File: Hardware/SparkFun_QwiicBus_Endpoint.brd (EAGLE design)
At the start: 44.5 x 25.4 mm, 68 parts, among them J1 QWIIC, J2 QWIIC, J3 RJ45, U1 PCA9615

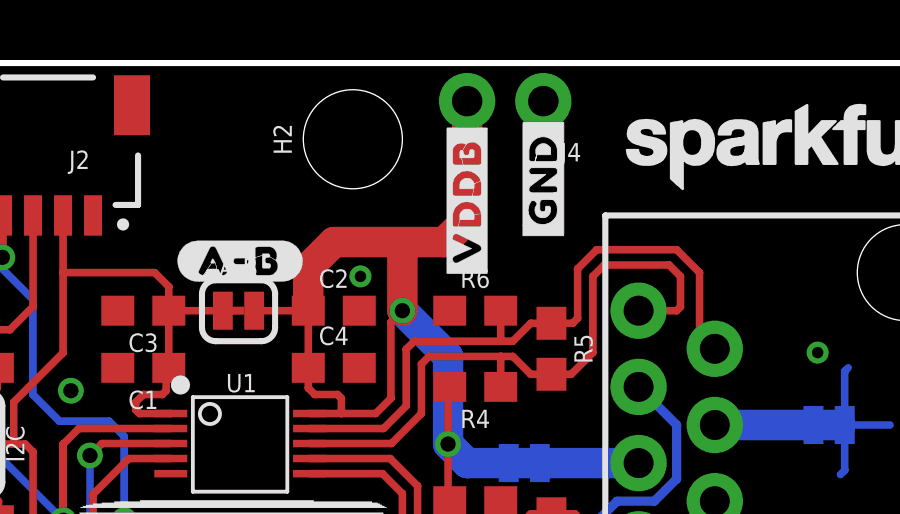
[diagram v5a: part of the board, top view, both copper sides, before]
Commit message: changing labels on grn pair, removing vddb
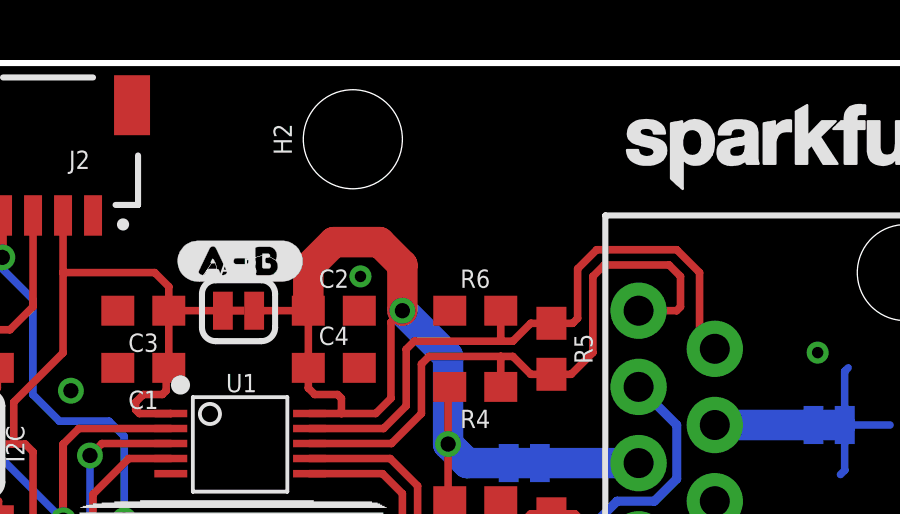
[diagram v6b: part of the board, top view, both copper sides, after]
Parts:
- removed J4: (no value), SparkFun-Connectors:1X02_NO_SILK
- removed U$12, U$13: (no value), output:#VDDB#0
- removed U$20: (no value), output:#GRNW#0
- removed U$22: (no value), output:#GRN#0
- U$2, U$3: device output:#GND#0 -> output:#HV##0
- moved U$3 22.1 mm to (26.7, 1.78), turned to 90 degrees
- moved U$2 17.5 mm to (29.2, 1.78), flipped to the bottom
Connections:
- net GND: no longer J4.1
- net VDD_B: no longer J4.2
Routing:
- net VDD_B: track 37.3 -> 30.5 mm
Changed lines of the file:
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@@
 <attribute name="VALUE" x="4.572" y="22.86" size="0.6096" layer="27" font="vector" ratio="20" rot="R90" align="top-center"/>
-</element>
-<element name="J4" library="SparkFun-Connectors" package="1X02_NO_SILK" value="" x="29.21" y="24.13" smashed="yes" rot="R180">
-<attribute name="NAME" x="30.48" y="22.733" size="0.6096" layer="25" font="vector" ratio="20" rot="R180"/>
-<attribute name="VALUE" x="30.48" y="26.162" size="0.6096" layer="27" font="vector" ratio="20" rot="R180"/>
 </element>
 <element name="LOGO1" library="SparkFun-Aesthetics" package="OSHW-LOGO-M" value="OSHW-LOGOM" x="12.7" y="2.54" smashed="yes" rot="MR0"/>
@@
 <attribute name="VALUE" x="25.4" y="-0.762" size="0.6096" layer="27" font="vector" ratio="20"/>
 </element>
-<element name="U$2" library="output" package="#GND#0" value="" x="29.21" y="19.304" smashed="yes" rot="R90"/>
-<element name="U$3" library="output" package="#GND#0" value="" x="29.21" y="23.749" smashed="yes" rot="MR270"/>
 <element name="U$4" library="output" package="#GND#0" value="" x="6.223" y="17.78" smashed="yes" rot="MR0"/>
 <element name="U$5" library="output" package="#GND#0" value="" x="1.778" y="17.78" smashed="yes"/>
@@
 <element name="U$10" library="output" package="#SCL#0" value="" x="1.778" y="10.16" smashed="yes"/>
 <element name="U$11" library="output" package="#EN#0" value="" x="1.778" y="7.62" smashed="yes"/>
-<element name="U$12" library="output" package="#VDDB#0" value="" x="26.67" y="18.034" smashed="yes" rot="R90"/>
-<element name="U$13" library="output" package="#VDDB#0" value="" x="26.67" y="18.034" smashed="yes" rot="MR90"/>
 <element name="U$14" library="output" package="#VDDB#0" value="" x="28.575" y="18.288" smashed="yes" rot="MR270"/>
 <element name="U$15" library="output" package="#SDA#0" value="" x="6.223" y="12.7" smashed="yes" rot="MR0"/>
@@
 <element name="U$18" library="output" package="#A#B#0" value="" x="17.018" y="18.796" smashed="yes"/>
 <element name="U$19" library="output" package="#GRNW#0" value="" x="29.21" y="1.905" smashed="yes" rot="R90"/>
-<element name="U$20" library="output" package="#GRNW#0" value="" x="29.21" y="7.747" smashed="yes" rot="MR270"/>
 <element name="U$21" library="output" package="#GRN#0" value="" x="26.67" y="2.032" smashed="yes" rot="R90"/>
-<element name="U$22" library="output" package="#GRN#0" value="" x="26.67" y="6.35" smashed="yes" rot="MR270"/>
 <element name="U$25" library="output" package="ENDPOINT0" value="" x="30.48" y="2.54" smashed="yes"/>
 <element name="U$26" library="output" package="ENDPOINT0" value="" x="25.781" y="9.525" smashed="yes" rot="MR0"/>
@@
 <element name="U$28" library="QwiicBus#working#Logo#jpg (2)" package="QWIICBUS#WORKING#LOGO#JPG" value="" x="19.558" y="8.509" smashed="yes"/>
 <element name="U$23" library="QwiicBus#working#Logo#jpg (2)" package="QWIICBUS#WORKING#LOGO#JPG" value="" x="18.442" y="13.874" smashed="yes" rot="MR0"/>
+<element name="U$2" library="output" package="#HV##0" value="" x="29.21" y="1.778" smashed="yes" rot="MR90"/>
+<element name="U$3" library="output" package="#HV##0" value="" x="26.67" y="1.778" smashed="yes" rot="MR90"/>
 </elements>
 <signals>
@@
 </polygon>
 <contactref element="GND" pad="1"/>
-<contactref element="J4" pad="1"/>
 <via x="10.795" y="6.604" extent="1-16" drill="0.508"/>
 <via x="5.207" y="5.715" extent="1-16" drill="0.381"/>
@@
 <contactref element="C4" pad="1"/>
 <contactref element="A-B" pad="2"/>
-<contactref element="J4" pad="2"/>
 <wire x1="19.5707" y1="17.3863" x2="19.812" y2="17.145" width="0.254" layer="1"/>
 <wire x1="19.812" y1="17.145" x2="21.375" y2="17.145" width="0.254" layer="1"/>
@@
 <wire x1="22.225" y1="19.431" x2="21.375" y2="18.581" width="1.016" layer="1"/>
 <wire x1="21.375" y1="18.581" x2="21.375" y2="17.145" width="1.016" layer="1"/>
-<wire x1="22.225" y1="19.431" x2="24.511" y2="19.431" width="1.016" layer="1"/>
-<wire x1="24.511" y1="19.431" x2="25.908" y2="19.431" width="1.016" layer="1"/>
-<wire x1="25.908" y1="19.431" x2="26.67" y2="20.193" width="1.016" layer="1"/>
-<wire x1="26.67" y1="20.193" x2="26.67" y2="24.13" width="1.016" layer="1"/>
+<wire x1="24.511" y1="17.145" x2="24.511" y2="18.669" width="1.016" layer="1"/>
+<wire x1="24.511" y1="18.669" x2="23.749" y2="19.431" width="1.016" layer="1"/>
+<wire x1="23.749" y1="19.431" x2="22.225" y2="19.431" width="1.016" layer="1"/>
 <wire x1="24.13" y1="14.224" x2="24.13" y2="16.764" width="0.254" layer="1"/>
 <wire x1="24.13" y1="16.764" x2="24.511" y2="17.145" width="0.254" layer="1"/>
 <wire x1="26.035" y1="15.621" x2="24.511" y2="17.145" width="1.016" layer="16"/>
 <wire x1="19.5707" y1="17.145" x2="19.5707" y2="17.3863" width="0.254" layer="1"/>
-<wire x1="24.511" y1="17.145" x2="24.511" y2="19.431" width="1.016" layer="1"/>
 </signal>
 <signal name="EN">

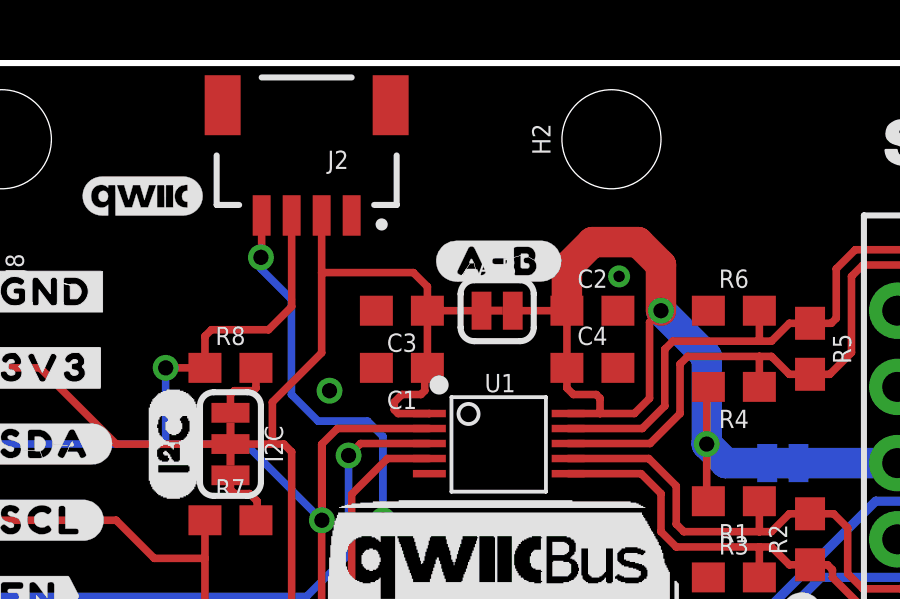
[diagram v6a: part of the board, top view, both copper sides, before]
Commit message: making everything 3v3
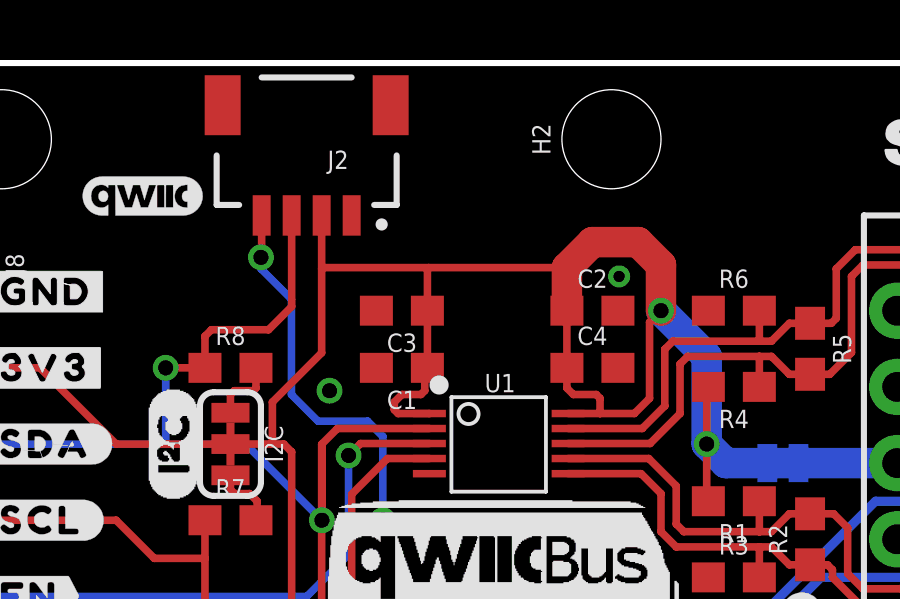
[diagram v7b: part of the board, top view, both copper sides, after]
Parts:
- removed A-B: JUMPER, SparkFun-Jumpers:SMT-JUMPER_2_NC_TRACE_SILK
- removed U$18: (no value), output:#A#B#0
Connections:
- removed net VDD_A: A-B.1, C1.1, C3.1, D11.A, I2C.2, J1.2, J2.2, J8.2, U1.1
- removed net VDD_B: A-B.2, C2.1, C4.1, R1.2, R4.2, U1.10, VDDB.1
- new net 3.3V: C1.1, C2.1, C3.1, C4.1, D11.A, I2C.2, J1.2, J2.2, J8.2, R1.2, R4.2, U1.1, U1.10, VDDB.1
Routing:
- net 3.3V: track 0.00 -> 79.9 mm, vias 0 -> 4
- net VDD_A: track 48.6 -> 0.00 mm, vias 2 -> 0
- net VDD_B: track 30.5 -> 0.00 mm, vias 2 -> 0
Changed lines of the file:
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@@
 <attribute name="VALUE" x="22.225" y="14.478" size="0.6096" layer="27" font="vector" ratio="20" align="top-center"/>
-</element>
-<element name="A-B" library="SparkFun-Jumpers" package="SMT-JUMPER_2_NC_TRACE_SILK" package3d_urn="urn:adsk.eagle:package:39281/1" value="JUMPER" x="19.05" y="17.145" smashed="yes">
-<attribute name="NAME" x="19.05" y="18.288" size="0.6096" layer="25" font="vector" ratio="20" align="bottom-center"/>
-<attribute name="VALUE" x="19.05" y="16.002" size="0.6096" layer="27" font="vector" ratio="20" align="top-center"/>
 </element>
 <element name="J3" library="SparkFun-Connectors" package="RJ45-8" value="RJ45" x="41.275" y="12.7" smashed="yes" rot="R90">
@@
 <element name="U$16" library="output" package="#SCL#0" value="" x="5.969" y="10.16" smashed="yes" rot="MR0"/>
 <element name="U$17" library="output" package="#EN#0" value="" x="5.08" y="7.62" smashed="yes" rot="MR0"/>
-<element name="U$18" library="output" package="#A#B#0" value="" x="17.018" y="18.796" smashed="yes"/>
 <element name="U$19" library="output" package="#GRNW#0" value="" x="29.21" y="1.905" smashed="yes" rot="R90"/>
 <element name="U$21" library="output" package="#GRN#0" value="" x="26.67" y="2.032" smashed="yes" rot="R90"/>
@@
 <wire x1="39.2557" y1="11.8237" x2="39.116" y2="11.684" width="0.254" layer="16"/>
 </signal>
-<signal name="VDD_A">
-<contactref element="J1" pad="2"/>
-<contactref element="J2" pad="2"/>
-<contactref element="U1" pad="1"/>
-<contactref element="C1" pad="1"/>
-<contactref element="C3" pad="1"/>
-<contactref element="A-B" pad="1"/>
-<contactref element="I2C" pad="2"/>
-<wire x1="11.557" y1="12.7" x2="11.938" y2="12.7" width="0.254" layer="1"/>
-<wire x1="12.2" y1="5.08" x2="12.2" y2="6.604" width="0.254" layer="1"/>
-<wire x1="12.2" y1="6.604" x2="12.2" y2="12.438" width="0.254" layer="1"/>
-<wire x1="12.2" y1="12.438" x2="11.938" y2="12.7" width="0.254" layer="1"/>
-<wire x1="11.557" y1="14.097" x2="11.557" y2="12.7" width="0.254" layer="1"/>
-<wire x1="18.5293" y1="17.3863" x2="18.288" y2="17.145" width="0.254" layer="1"/>
-<wire x1="18.288" y1="17.145" x2="16.725" y2="17.145" width="0.254" layer="1"/>
-<wire x1="16.637" y1="14.478" x2="16.51" y2="14.351" width="0.254" layer="1"/>
-<wire x1="16.51" y1="14.351" x2="15.875" y2="14.351" width="0.254" layer="1"/>
-<wire x1="15.875" y1="14.351" x2="15.621" y2="14.097" width="0.254" layer="1"/>
-<wire x1="15.621" y1="14.097" x2="15.621" y2="13.843" width="0.254" layer="1"/>
-<wire x1="15.621" y1="13.843" x2="15.748" y2="13.716" width="0.254" layer="1"/>
-<wire x1="15.748" y1="13.716" x2="16.7895" y2="13.716" width="0.254" layer="1"/>
-<wire x1="16.7895" y1="13.716" x2="16.791" y2="13.7175" width="0.254" layer="1"/>
-<wire x1="16.725" y1="15.24" x2="16.725" y2="17.145" width="0.254" layer="1"/>
-<wire x1="16.637" y1="14.478" x2="16.637" y2="15.152" width="0.254" layer="1"/>
-<wire x1="16.637" y1="15.152" x2="16.725" y2="15.24" width="0.254" layer="1"/>
-<wire x1="10.16" y1="12.7" x2="11.557" y2="12.7" width="0.254" layer="1"/>
-<wire x1="11.557" y1="14.097" x2="13.2" y2="15.74" width="0.254" layer="1"/>
-<wire x1="13.2" y1="18.415" x2="13.2" y2="20.32" width="0.254" layer="1"/>
-<wire x1="13.2" y1="15.74" x2="13.2" y2="18.415" width="0.254" layer="1"/>
-<wire x1="13.2" y1="18.415" x2="16.256" y2="18.415" width="0.254" layer="1"/>
-<wire x1="16.256" y1="18.415" x2="16.725" y2="17.946" width="0.254" layer="1"/>
-<wire x1="16.725" y1="17.946" x2="16.725" y2="17.145" width="0.254" layer="1"/>
-<wire x1="10.16" y1="12.7" x2="6.35" y2="12.7" width="0.254" layer="1"/>
-<wire x1="6.35" y1="12.7" x2="3.81" y2="15.24" width="0.254" layer="1"/>
-<contactref element="D11" pad="A"/>
-<wire x1="7.989" y1="1.27" x2="8.89" y2="2.171" width="0.2032" layer="1"/>
-<wire x1="8.89" y1="2.171" x2="8.89" y2="2.794" width="0.2032" layer="1"/>
-<wire x1="8.89" y1="2.794" x2="9.2329" y2="3.1369" width="0.2032" layer="1"/>
-<wire x1="9.2329" y1="3.1369" x2="12.192" y2="3.1369" width="0.2032" layer="1"/>
-<via x="12.192" y="3.1369" extent="1-16" drill="0.381"/>
-<wire x1="12.192" y1="3.1369" x2="12.192" y2="6.596" width="0.2032" layer="16"/>
-<wire x1="12.192" y1="6.596" x2="12.2" y2="6.604" width="0.2032" layer="16"/>
-<via x="12.2" y="6.604" extent="1-16" drill="0.381"/>
-<wire x1="18.5293" y1="17.145" x2="18.5293" y2="17.3863" width="0.254" layer="1"/>
-<contactref element="J8" pad="2"/>
-<wire x1="3.81" y1="15.24" x2="1.27" y2="15.24" width="0.254" layer="1"/>
-</signal>
-<signal name="VDD_B">
+<signal name="3.3V">
 <contactref element="U1" pad="10"/>
 <contactref element="R1" pad="2"/>
@@
 <contactref element="C2" pad="1"/>
 <contactref element="C4" pad="1"/>
-<contactref element="A-B" pad="2"/>
-<wire x1="19.5707" y1="17.3863" x2="19.812" y2="17.145" width="0.254" layer="1"/>
-<wire x1="19.812" y1="17.145" x2="21.375" y2="17.145" width="0.254" layer="1"/>
 <wire x1="21.416" y1="13.7175" x2="22.479" y2="13.7175" width="0.254" layer="1"/>
 <wire x1="22.479" y1="14.224" x2="22.479" y2="13.7175" width="0.254" layer="1"/>
@@
 <wire x1="26.67" y1="12.065" x2="26.035" y2="12.7" width="1.016" layer="16"/>
 <wire x1="26.035" y1="15.621" x2="26.035" y2="12.7" width="1.016" layer="16"/>
-<wire x1="22.225" y1="19.431" x2="21.375" y2="18.581" width="1.016" layer="1"/>
-<wire x1="21.375" y1="18.581" x2="21.375" y2="17.145" width="1.016" layer="1"/>
+<wire x1="21.375" y1="17.145" x2="21.375" y2="18.581" width="1.016" layer="1"/>
 <wire x1="24.511" y1="17.145" x2="24.511" y2="18.669" width="1.016" layer="1"/>
 <wire x1="24.511" y1="18.669" x2="23.749" y2="19.431" width="1.016" layer="1"/>
@@
 <wire x1="24.13" y1="16.764" x2="24.511" y2="17.145" width="0.254" layer="1"/>
 <wire x1="26.035" y1="15.621" x2="24.511" y2="17.145" width="1.016" layer="16"/>
-<wire x1="19.5707" y1="17.145" x2="19.5707" y2="17.3863" width="0.254" layer="1"/>
+<contactref element="J1" pad="2"/>
+<contactref element="J2" pad="2"/>
+<contactref element="U1" pad="1"/>
+<contactref element="C1" pad="1"/>
+<contactref element="C3" pad="1"/>
+<contactref element="I2C" pad="2"/>
+<wire x1="11.557" y1="12.7" x2="11.938" y2="12.7" width="0.254" layer="1"/>
+<wire x1="12.2" y1="5.08" x2="12.2" y2="6.604" width="0.254" layer="1"/>
+<wire x1="12.2" y1="6.604" x2="12.2" y2="12.438" width="0.254" layer="1"/>
+<wire x1="12.2" y1="12.438" x2="11.938" y2="12.7" width="0.254" layer="1"/>
+<wire x1="11.557" y1="14.097" x2="11.557" y2="12.7" width="0.254" layer="1"/>
+<wire x1="16.637" y1="14.478" x2="16.51" y2="14.351" width="0.254" layer="1"/>
+<wire x1="16.51" y1="14.351" x2="15.875" y2="14.351" width="0.254" layer="1"/>
+<wire x1="15.875" y1="14.351" x2="15.621" y2="14.097" width="0.254" layer="1"/>
+<wire x1="15.621" y1="14.097" x2="15.621" y2="13.843" width="0.254" layer="1"/>
+<wire x1="15.621" y1="13.843" x2="15.748" y2="13.716" width="0.254" layer="1"/>
+<wire x1="15.748" y1="13.716" x2="16.7895" y2="13.716" width="0.254" layer="1"/>
+<wire x1="16.7895" y1="13.716" x2="16.791" y2="13.7175" width="0.254" layer="1"/>
+<wire x1="16.725" y1="15.24" x2="16.725" y2="17.145" width="0.254" layer="1"/>
+<wire x1="16.637" y1="14.478" x2="16.637" y2="15.152" width="0.254" layer="1"/>
+<wire x1="16.637" y1="15.152" x2="16.725" y2="15.24" width="0.254" layer="1"/>
+<wire x1="10.16" y1="12.7" x2="11.557" y2="12.7" width="0.254" layer="1"/>
+<wire x1="11.557" y1="14.097" x2="13.2" y2="15.74" width="0.254" layer="1"/>
+<wire x1="13.2" y1="15.74" x2="13.2" y2="18.542" width="0.254" layer="1"/>
+<wire x1="13.2" y1="18.542" x2="13.2" y2="20.32" width="0.254" layer="1"/>
+<wire x1="10.16" y1="12.7" x2="6.35" y2="12.7" width="0.254" layer="1"/>
+<wire x1="6.35" y1="12.7" x2="3.81" y2="15.24" width="0.254" layer="1"/>
+<contactref element="D11" pad="A"/>
+<wire x1="7.989" y1="1.27" x2="8.89" y2="2.171" width="0.2032" layer="1"/>
+<wire x1="8.89" y1="2.171" x2="8.89" y2="2.794" width="0.2032" layer="1"/>
+<wire x1="8.89" y1="2.794" x2="9.2329" y2="3.1369" width="0.2032" layer="1"/>
+<wire x1="9.2329" y1="3.1369" x2="12.192" y2="3.1369" width="0.2032" layer="1"/>
+<via x="12.192" y="3.1369" extent="1-16" drill="0.381"/>
+<wire x1="12.192" y1="3.1369" x2="12.192" y2="6.596" width="0.2032" layer="16"/>
+<wire x1="12.192" y1="6.596" x2="12.2" y2="6.604" width="0.2032" layer="16"/>
+<via x="12.2" y="6.604" extent="1-16" drill="0.381"/>
+<contactref element="J8" pad="2"/>
+<wire x1="3.81" y1="15.24" x2="1.27" y2="15.24" width="0.254" layer="1"/>
+<wire x1="22.225" y1="19.431" x2="21.375" y2="18.581" width="1.016" layer="1"/>
+<wire x1="21.326" y1="18.63" x2="21.375" y2="18.581" width="0.254" layer="1"/>
+<wire x1="21.375" y1="18.581" x2="16.764" y2="18.581" width="0.254" layer="1"/>
+<wire x1="16.764" y1="18.581" x2="13.239" y2="18.581" width="0.254" layer="1"/>
+<wire x1="13.239" y1="18.581" x2="13.2" y2="18.542" width="0.254" layer="1"/>
+<wire x1="16.725" y1="17.145" x2="16.725" y2="18.542" width="0.254" layer="1"/>
+<wire x1="16.725" y1="18.542" x2="16.764" y2="18.581" width="0.254" layer="1"/>
 </signal>
 <signal name="EN">
